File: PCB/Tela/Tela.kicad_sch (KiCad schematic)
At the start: 9 parts

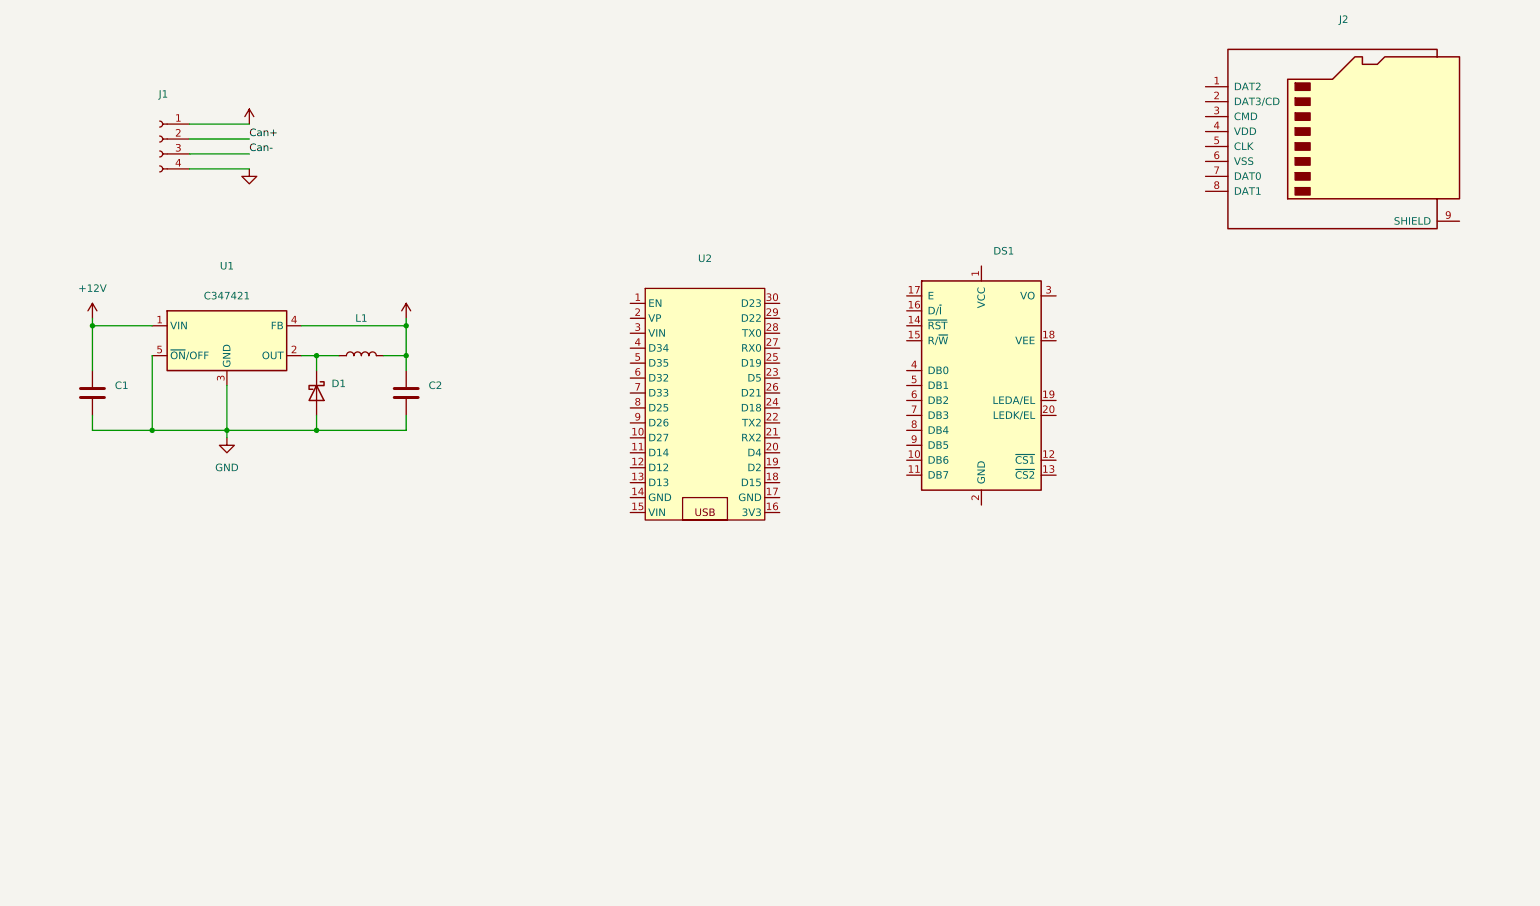
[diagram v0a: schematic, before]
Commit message: adição dos footprint do modulo de can, adição dos botoes, e desenho de areas no silkscreen
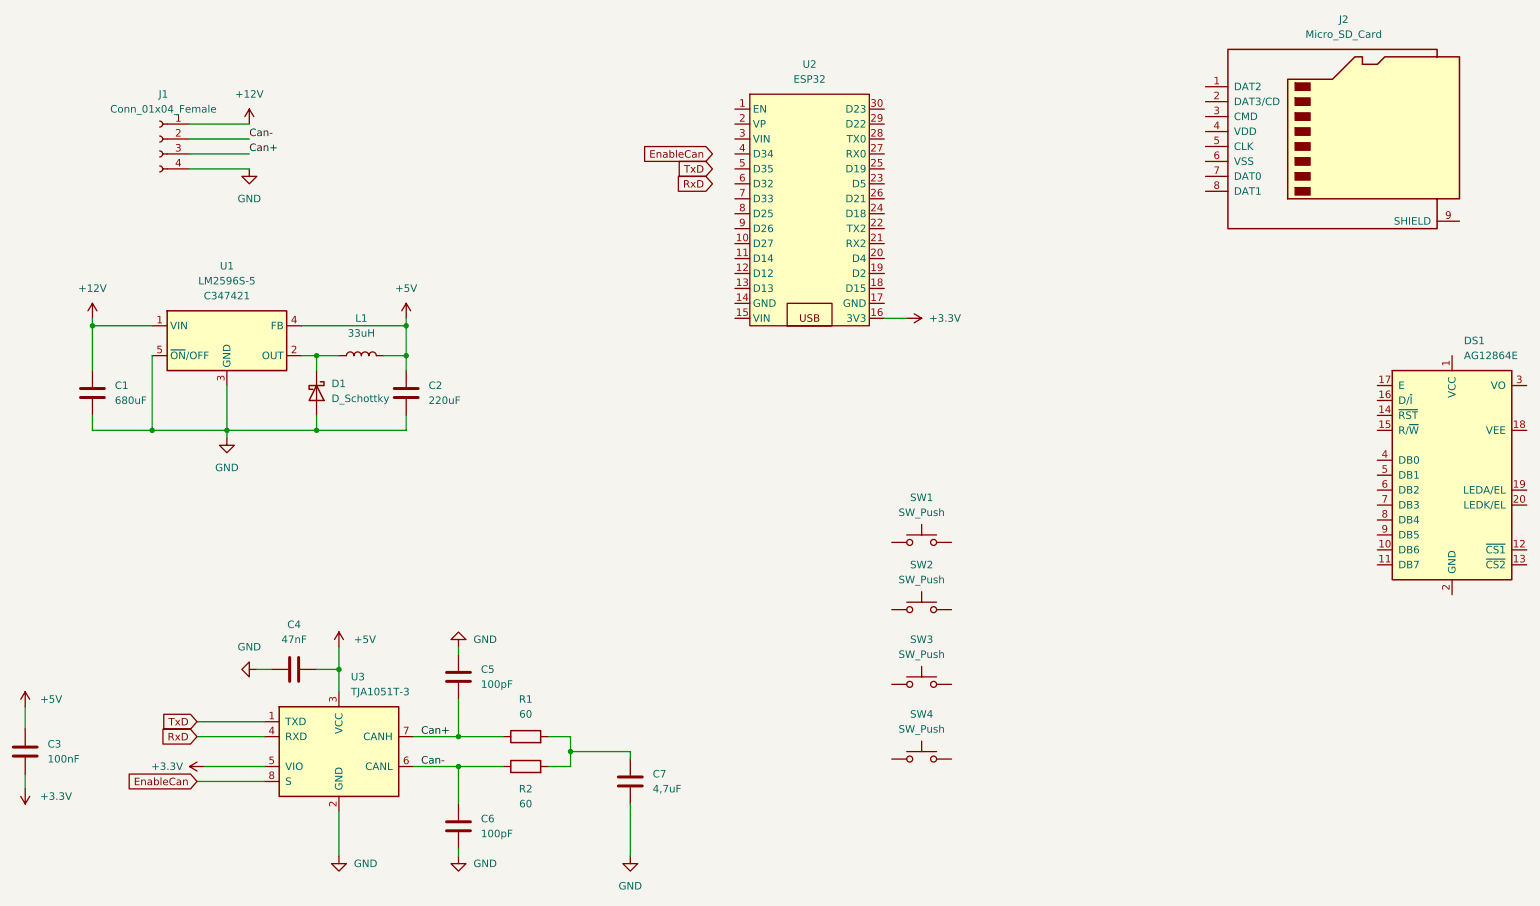
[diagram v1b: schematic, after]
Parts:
- added C3: 100nF, Capacitor_SMD:C_0603_1608Metric_Pad1.08x0.95mm_HandSolder, symbol Device:C
- added C4: 47nF, Capacitor_SMD:C_0603_1608Metric_Pad1.08x0.95mm_HandSolder, symbol Device:C
- added C5, C6: 100pF, Capacitor_SMD:C_0603_1608Metric_Pad1.08x0.95mm_HandSolder, symbol Device:C
- added C7: 4,7uF, Capacitor_SMD:C_0603_1608Metric_Pad1.08x0.95mm_HandSolder, symbol Device:C
- added R1, R2: 60, Resistor_SMD:R_0603_1608Metric_Pad0.98x0.95mm_HandSolder, symbol Device:R
- added SW1, SW2, SW3, SW4: SW_Push, Button_Switch_SMD:SW_SPST_PTS645, symbol Switch:SW_Push
- added U3: TJA1051T-3, Package_SO:SOIC-8_3.9x4.9mm_P1.27mm, symbol Interface_CAN_LIN:TJA1051T-3
- C1: value (none) -> 680uF; footprint (none) -> Capacitor_SMD:CP_Elec_10x10.5
- C2: value (none) -> 220uF; footprint (none) -> Capacitor_SMD:CP_Elec_6.3x5.4
- D1: value (none) -> D_Schottky; footprint (none) -> Diode_SMD:D_SMB
- DS1: value (none) -> AG12864E; footprint (none) -> Display:AG12864E
- J1: value (none) -> Conn_01x04_Female; footprint (none) -> TerminalBlock_Phoenix:TerminalBlock_Phoenix_MKDS-1,5-4-5.08_1x04_P5.08mm_Horizontal
- J2: value (none) -> Micro_SD_Card; footprint (none) -> Connector_Card:microSD_HC_Hirose_DM3D-SF
- L1: value (none) -> 33uH; footprint (none) -> Inductor_SMD:L_12x12mm_H8mm
- U1: value (none) -> LM2596S-5; footprint (none) -> Package_TO_SOT_SMD:TO-263-5_TabPin3
- U2: value (none) -> ESP32; footprint (none) -> Library:ESP32_DevKit
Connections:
- net +5V: now also C3.2, C4.1, U3.3 (VCC)
- net Can+: now also J1.3 (Pin_3), C5.2, R1.1, U3.7 (CANH); no longer J1.2 (Pin_2)
- net Can-: now also J1.2 (Pin_2), C6.2, R2.1, U3.6 (CANL); no longer J1.3 (Pin_3)
- net GND: now also C4.2, C5.1, C6.1, C7.1, U3.2 (GND)
- net +3.3V: now reaches U2.16 (3V3)
- net +3.3V: now also C3.1, U3.5 (VIO)
- new net: C7.2, R1.2, R2.2
- new net EnableCan: U3.8 (S)
- new net RxD: U3.4 (RXD)
- new net TxD: U3.1 (TXD)
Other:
- moved on the sheet: DS1, U2
